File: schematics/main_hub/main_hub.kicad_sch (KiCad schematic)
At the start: 41 parts, among them J1 Conn_02x25_Counter_Clockwise, J2 Conn_02x25_Counter_Clockwise, J3 Conn_02x25_Counter_Clockwise, J4 Conn_02x25_Counter_Clockwise

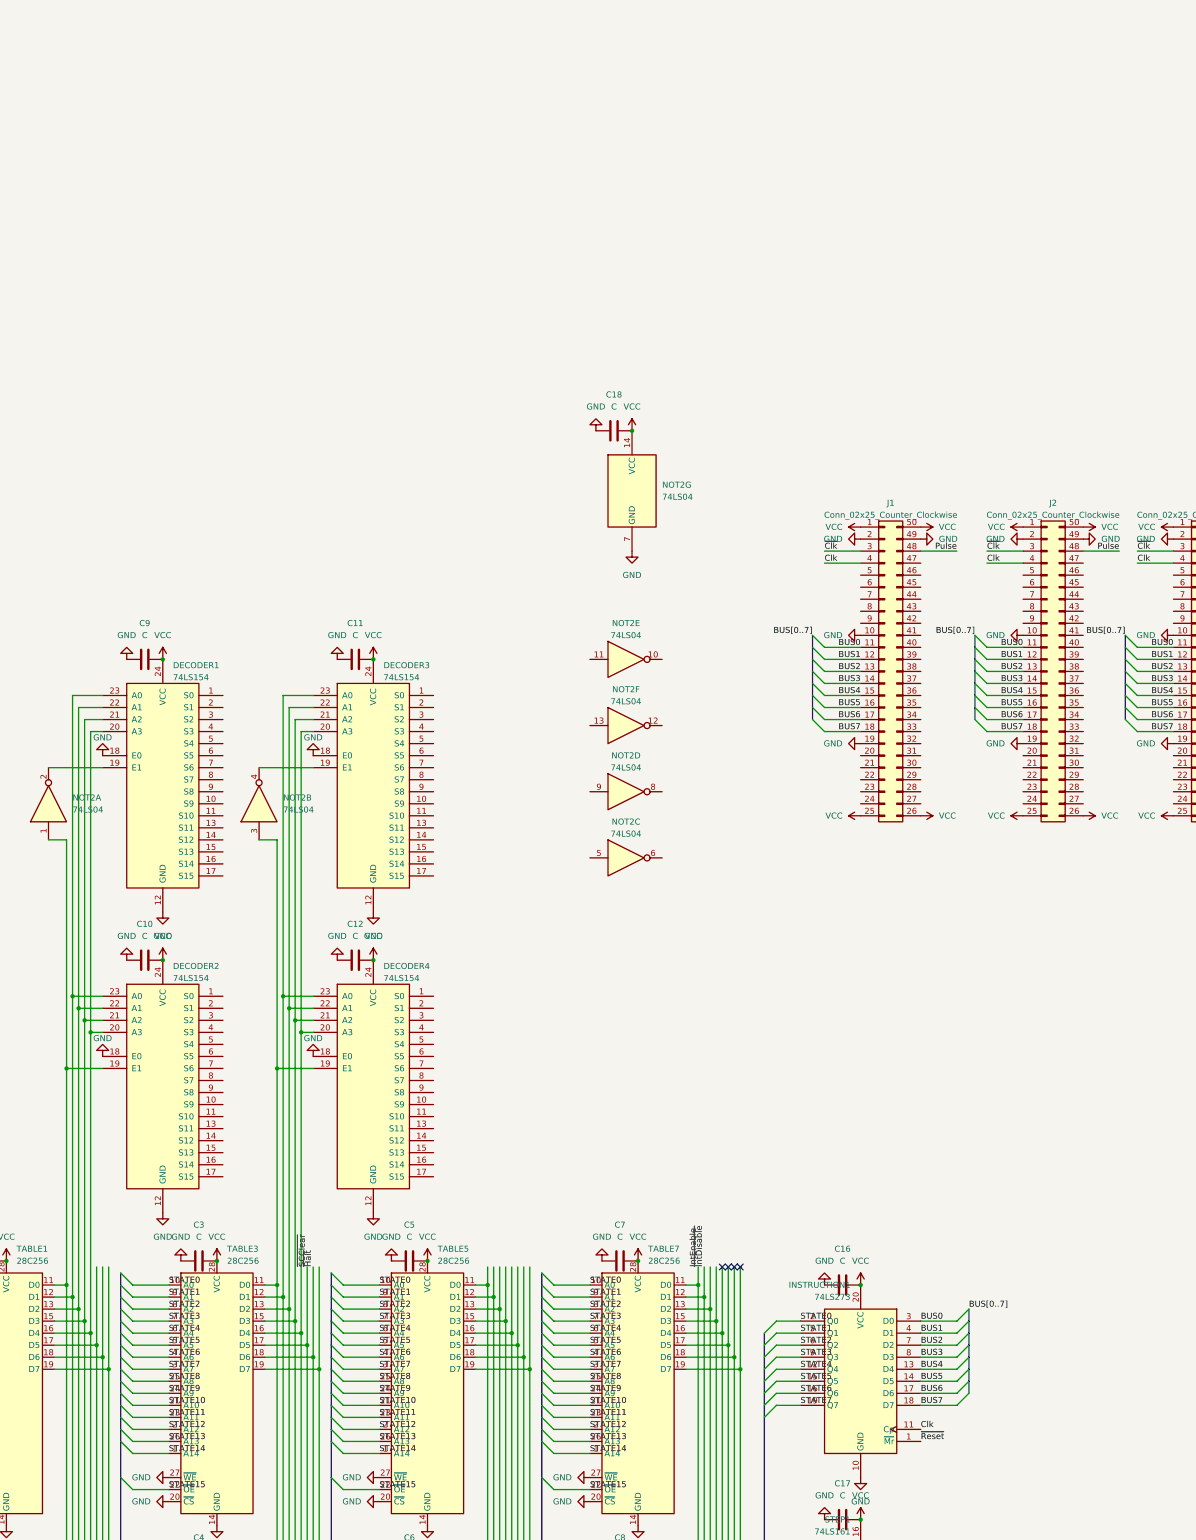
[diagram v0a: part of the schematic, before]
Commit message: Add more labels to main hub decoder
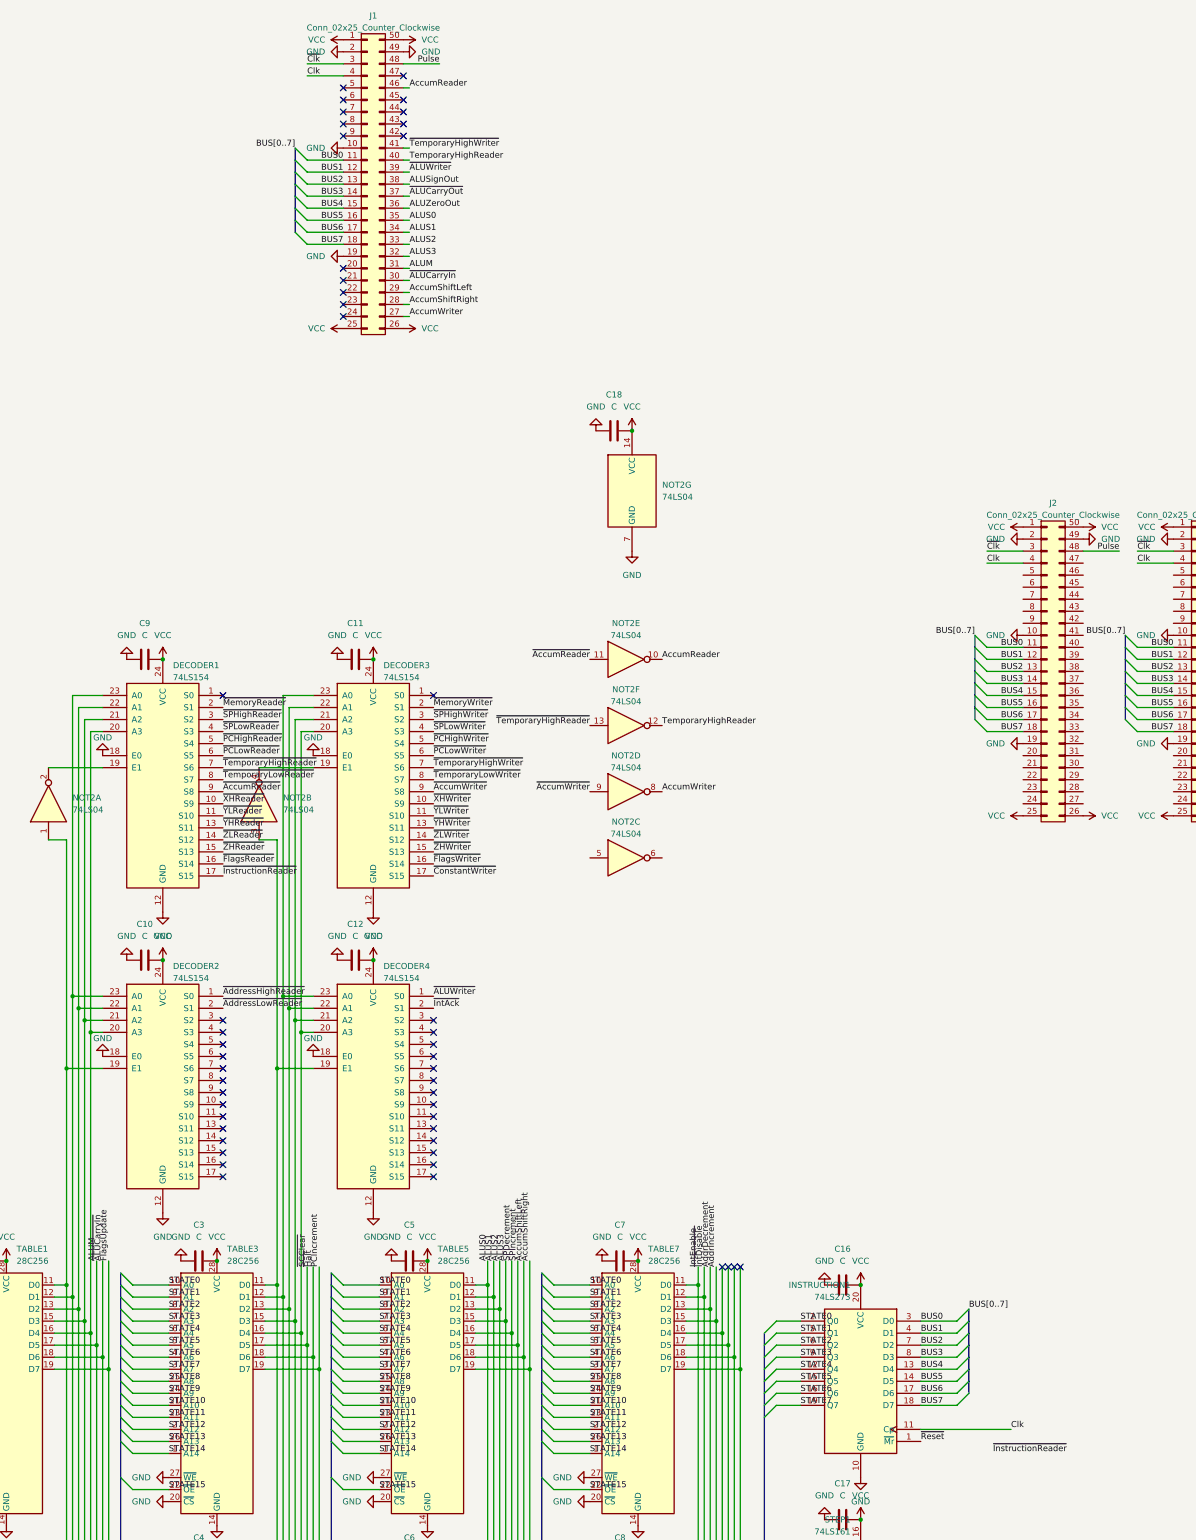
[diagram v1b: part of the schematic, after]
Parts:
- J1, J2, J3, J4: footprint Connector_IDC:IDC-Header_2x25_P2.54mm_Latch_Vertical -> Connector_PinHeader_2.54mm:PinHeader_2x25_P2.54mm_Vertical
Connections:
- net ALUS0: now reaches TABLE5.11 (D0), TABLE6.11 (D0)
- net ALUS0: now also J1.35 (Pin_35)
- net ALUS1: now reaches TABLE5.12 (D1), TABLE6.12 (D1)
- net ALUS1: now also J1.34 (Pin_34)
- net ALUS2: now reaches TABLE5.13 (D2), TABLE6.13 (D2)
- net ALUS2: now also J1.33 (Pin_33)
- net ALUS3: now reaches TABLE5.15 (D3), TABLE6.15 (D3)
- net ALUS3: now also J1.32 (Pin_32)
- net SPDecrement: now reaches TABLE5.16 (D4), TABLE6.16 (D4)
- net SPIncrement: now reaches TABLE5.17 (D5), TABLE6.17 (D5)
- net AccumShiftLeft: now reaches TABLE5.18 (D6), TABLE6.18 (D6)
- net AccumShiftLeft: now also J1.29 (Pin_29)
- net AccumShiftRight: now reaches TABLE5.19 (D7), TABLE6.19 (D7)
- net AccumShiftRight: now also J1.28 (Pin_28)
- net AddrDecrement: now reaches TABLE7.13 (D2), TABLE8.13 (D2)
- net AddrIncrement: now reaches TABLE7.15 (D3), TABLE8.15 (D3)
- net ~{ALUWriter}: now reaches DECODER4.1 (S0)
- net ~{ALUWriter}: now also J1.39 (Pin_39)
- net ~{IntAck}: now reaches DECODER4.2 (S1)
- net AccumWriter: now reaches J1.27 (Pin_27)
- net AccumWriter: now also NOT2.8
- net ~{ALUCarryIn}: now reaches J1.30 (Pin_30)
- net ~{ALUCarryIn}: now also TABLE1.18 (D6), TABLE2.18 (D6)
- net ALUM: now reaches J1.31 (Pin_31)
- net ALUM: now also TABLE1.17 (D5), TABLE2.17 (D5)
- net ALUZeroOut: now reaches J1.36 (Pin_36)
- net ~{ALUCarryOut}: now reaches J1.37 (Pin_37)
- net ALUSignOut: now reaches J1.38 (Pin_38)
- net TemporaryHighReader: now reaches J1.40 (Pin_40)
- net TemporaryHighReader: now also NOT2.12
- net ~{TemporaryHighWriter}: now reaches J1.41 (Pin_41)
- net ~{TemporaryHighWriter}: now also DECODER3.7 (S6)
- net AccumReader: now reaches J1.46 (Pin_46)
- net AccumReader: now also NOT2.10
- net ~{AddressHighReader}: now reaches DECODER2.1 (S0)
- net ~{AddressLowReader}: now reaches DECODER2.2 (S1)
- net ~{AccumReader}: now reaches NOT2.11
- net ~{AccumReader}: now also DECODER1.9 (S8)
- net PCIncrement: now reaches TABLE3.19 (D7), TABLE4.19 (D7)
- net ~{XHReader}: now reaches DECODER1.10 (S9)
- net ~{YLReader}: now reaches DECODER1.11 (S10)
- net ~{YHReader}: now reaches DECODER1.13 (S11)
- net ~{ZLReader}: now reaches DECODER1.14 (S12)
- net ~{ZHReader}: now reaches DECODER1.15 (S13)
- net ~{FlagsReader}: now reaches DECODER1.16 (S14)
- net ~{InstructionReader}: now reaches DECODER1.17 (S15)
- net ~{MemoryReader}: now reaches DECODER1.2 (S1)
- net ~{SPHighReader}: now reaches DECODER1.3 (S2)
- net ~{SPLowReader}: now reaches DECODER1.4 (S3)
- net ~{PCHighReader}: now reaches DECODER1.5 (S4)
- net ~{PCLowReader}: now reaches DECODER1.6 (S5)
- net ~{TemporaryHighReader}: now reaches DECODER1.7 (S6)
- net ~{TemporaryHighReader}: now also NOT2.13
- net ~{TemporaryLowReader}: now reaches DECODER1.8 (S7)
- net FlagsUpdate: now reaches TABLE1.19 (D7), TABLE2.19 (D7)
- net ~{AccumWriter}: now reaches NOT2.9
- net ~{AccumWriter}: now also DECODER3.9 (S8)
- net ~{XHWriter}: now reaches DECODER3.10 (S9)
- net ~{YLWriter}: now reaches DECODER3.11 (S10)
- net ~{YHWriter}: now reaches DECODER3.13 (S11)
- net ~{ZLWriter}: now reaches DECODER3.14 (S12)
- net ~{ZHWriter}: now reaches DECODER3.15 (S13)
- net ~{FlagsWriter}: now reaches DECODER3.16 (S14)
- net ~{ConstantWriter}: now reaches DECODER3.17 (S15)
- net ~{MemoryWriter}: now reaches DECODER3.2 (S1)
- net ~{SPHighWriter}: now reaches DECODER3.3 (S2)
- net ~{SPLowWriter}: now reaches DECODER3.4 (S3)
- net ~{PCHighWriter}: now reaches DECODER3.5 (S4)
- net ~{PCLowWriter}: now reaches DECODER3.6 (S5)
- net ~{TemporaryLowWriter}: now reaches DECODER3.8 (S7)
- no-connect marks 13 -> 58
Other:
- moved on the sheet: J1

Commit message: Connnect all modules together
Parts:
- removed NOT2: 74LS04, Package_DIP:DIP-14_W7.62mm_Socket_LongPads, symbol 74xx:74LS04
- added U1: 74LS02, Package_DIP:DIP-14_W7.62mm_Socket_LongPads, symbol 74xx:74LS02
- R1: footprint Resistor_THT:R_Axial_DIN0204_L3.6mm_D1.6mm_P5.08mm_Vertical -> (none)
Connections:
- net AccumReader is gone; now on net ~{AccumReader}: J1.46 (Pin_46)
- net AccumWriter is gone; now on net ~{AccumWriter}: J1.27 (Pin_27)
- net FlagsUpdate is gone; now on net ~{FlagsUpdate}: TABLE1.19 (D7), TABLE2.19 (D7)
- net TemporaryHighReader is gone; now on net ~{TemporaryHighReader}: J1.40 (Pin_40)
- net ALUSignOut: now also J2.23 (Pin_23)
- net ALUZeroOut: now also J2.21 (Pin_21)
- net Clk: no longer INSTRUCTION1.11 (Cp)
- net GND: now also U1.7 (GND)
- net STATE10: now also J2.46 (Pin_46)
- net STATE8: now also J2.44 (Pin_44)
- net STATE9: now also J2.45 (Pin_45)
- net VCC: now also U1.14 (VCC)
- net ~{ALUCarryOut}: now also J2.22 (Pin_22)
- net ~{Clk}: now also U1.2
- net ~{FlagsReader}: now also J2.34 (Pin_34)
- net ~{FlagsWriter}: now also J2.40 (Pin_40)
- net ~{InstructionReader}: now also U1.3
- net ~{XHReader}: now also J2.33 (Pin_33)
- net ~{XHWriter}: now also J2.39 (Pin_39)
- net ~{YHReader}: now also J2.31 (Pin_31)
- net ~{YHWriter}: now also J2.37 (Pin_37)
- net ~{YLReader}: now also J2.32 (Pin_32)
- net ~{YLWriter}: now also J2.38 (Pin_38)
- net ~{ZHReader}: now also J2.29 (Pin_29)
- net ~{ZHWriter}: now also J2.35 (Pin_35)
- net ~{ZLReader}: now also J2.30 (Pin_30)
- net ~{ZLWriter}: now also J2.36 (Pin_36)
- net ~{FlagsUpdate}: now reaches J2.28 (Pin_28)
- net at DECODER4.19 (E1), TABLE3.11 (D0), TABLE4.11 (D0): now also U1.5, U1.6
- net at DECODER2.19 (E1), TABLE1.11 (D0), TABLE2.11 (D0): now also U1.8, U1.9
- net at DECODER1.19 (E1): now also U1.10
- net at DECODER3.19 (E1): now also U1.4
- new net: INSTRUCTION1.11 (Cp), U1.1
- no-connect marks 58 -> 73
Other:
- moved on the sheet: C18, J2

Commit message: Add interface module schematic
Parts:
- added C19: C, symbol Device:C
- added U2: 74LS04, Package_DIP:DIP-14_W7.62mm_Socket_LongPads, symbol 74xx:74LS04
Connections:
- net GND: now also C19.2, U2.7 (GND)
- net Reset: now also J3.34 (Pin_34)
- net VCC: now also C19.1, U2.14 (VCC)
- net Wait: now also J3.37 (Pin_37)
- net ~{AddressHighReader}: now also U2.11
- net ~{AddressLowReader}: now also U2.13
- net ~{PCHighReader}: now also U2.5
- net ~{PCLowReader}: now also U2.9
- net ~{SPHighReader}: now also U2.1
- net ~{SPLowReader}: now also U2.3
- net IntAck: now reaches J3.35 (Pin_35)
- net IntReq: now reaches J3.36 (Pin_36)
- net Halt: now reaches J3.38 (Pin_38)
- net MemRead: now reaches J3.39 (Pin_39)
- net MemWrite: now reaches J3.40 (Pin_40)
- net AddrDec: now reaches J3.44 (Pin_44)
- net AddrInc: now reaches J3.45 (Pin_45)
- net AddrLowIn: now reaches J3.46 (Pin_46)
- net AddrLowIn: now also U2.12
- net AddrHighIn: now reaches J3.47 (Pin_47)
- net AddrHighIn: now also U2.10
- new net PCHighReader: U2.6
- new net PCLowReader: U2.8
- new net SPHighReader: U2.2
- new net SPLowReader: U2.4
- no-connect marks 73 -> 93
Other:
- moved on the sheet: C1, C10, C11, C12, C13, C14, C15, C16, C17, C18, C2, C3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
